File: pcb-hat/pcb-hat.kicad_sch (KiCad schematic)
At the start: 0 parts

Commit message: added SMD buzzer and current sensor
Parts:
- added R1: R_Shunt R010, symbol Device:R_Shunt
- added U1: INA219AxD, Package_SO:SOIC-8_3.9x4.9mm_P1.27mm, symbol Sensor_Energy:INA219AxD
- added U2: ~, symbol PiHatComponents:SMD_buzzer
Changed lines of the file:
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@@
 	(generator_version "9.0")
 	(paper "A4")
+	(symbol
+		(lib_id "Device:R_Shunt")
+		(at 128.27 78.74 0)
+		(unit 1)
+		(exclude_from_sim no)
+		(in_bom yes)
+		(on_board yes)
+		(dnp no)
+		(fields_autoplaced yes)
+		(property "Reference" "R1"
+			(at 125.73 77.4699 0)
+			(effects
+				(font
+					(size 1.27 1.27)
+				)
+				(justify right)
+			)
+		)
+		(property "Value" "R_Shunt R010"
+			(at 125.73 80.0099 0)
+			(effects
+				(font
+					(size 1.27 1.27)
+				)
+				(justify right)
+			)
+		)
+		(property "Footprint" ""
+			(at 126.492 78.74 90)
+			(effects
+				(font
+					(size 1.27 1.27)
+				)
+				(hide yes)
+			)
+		)
+		(property "Datasheet" "~"
+			(at 128.27 78.74 0)
+			(effects
+				(font
+					(size 1.27 1.27)
+				)
+				(hide yes)
+			)
+		)
+		(property "Description" "Shunt resistor with Kelvin connections"
+			(at 128.27 78.74 0)
+			(effects
+				(font
+					(size 1.27 1.27)
+				)
+				(hide yes)
+			)
+		)
+		(pin "2"
+		)
+		(pin "1"
+		)
+		(pin "3"
+		)
+		(pin "4"
+		)
+		(instances
+			(project ""
+				(path "/a3c2d30d-0751-4de7-a899-3d89ad40795d"
+					(reference "R1")
+					(unit 1)
+				)
+			)
+		)
+	)
+	(symbol
+		(lib_id "PiHatComponents:SMD_buzzer")
+		(at 116.84 99.06 0)
+		(unit 1)
+		(exclude_from_sim no)
+		(in_bom yes)
+		(on_board yes)
+		(dnp no)
+		(fields_autoplaced yes)
+		(property "Reference" "U2"
+			(at 133.35 97.1549 0)
+			(effects
+				(font
+					(size 1.27 1.27)
+				)
+				(justify left)
+			)
+		)
+		(property "Value" "~"
+			(at 133.35 99.6949 0)
+			(effects
+				(font
+					(size 1.27 1.27)
+				)
+				(justify left)
+			)
+		)
+		(property "Footprint" ""
+			(at 116.84 99.06 0)
+			(effects
+				(font
+					(size 1.27 1.27)
+				)
+				(hide yes)
+			)
+		)
+		(property "Datasheet" ""
+			(at 116.84 99.06 0)
+			(effects
+				(font
+					(size 1.27 1.27)
+				)
+				(hide yes)
+			)
+		)
+		(property "Description" ""
+			(at 116.84 99.06 0)
+			(effects
+				(font
+					(size 1.27 1.27)
+				)
+				(hide yes)
+			)
+		)
+		(pin "1"
+		)
+		(pin "2"
+		)
+		(instances
+			(project ""
+				(path "/a3c2d30d-0751-4de7-a899-3d89ad40795d"
+					(reference "U2")
+					(unit 1)
+				)
+			)
+		)
+	)
+	(symbol
+		(lib_id "Sensor_Energy:INA219AxD")
+		(at 95.25 78.74 0)
+		(unit 1)
+		(exclude_from_sim no)
+		(in_bom yes)
+		(on_board yes)
+		(dnp no)
+		(fields_autoplaced yes)
+		(property "Reference" "U1"
+			(at 97.3933 66.04 0)
+			(effects
+				(font
+					(size 1.27 1.27)
+				)
+				(justify left)
+			)
+		)
+		(property "Value" "INA219AxD"
+			(at 97.3933 68.58 0)
+			(effects
+				(font
+					(size 1.27 1.27)
+				)
+				(justify left)
+			)
+		)
+		(property "Footprint" "Package_SO:SOIC-8_3.9x4.9mm_P1.27mm"
+			(at 115.57 87.63 0)
+			(effects
+				(font
+					(size 1.27 1.27)
+				)
+				(hide yes)
+			)
+		)
+		(property "Datasheet" "http://www.ti.com/lit/ds/symlink/ina219.pdf"
+			(at 104.14 81.28 0)
+			(effects
+				(font
+					(size 1.27 1.27)
+				)
+				(hide yes)
+			)
+		)
+		(property "Description" "Zero-Drift, Bidirectional Current/Power Monitor (0-26V) With I2C Interface, SOIC-8"
+			(at 95.25 78.74 0)
+			(effects
+				(font
+					(size 1.27 1.27)
+				)
+				(hide yes)
+			)
+		)
+		(pin "8"
+		)
+		(pin "5"
+		)
+		(pin "6"
+		)
+		(pin "3"
+		)
+		(pin "4"
+		)
+		(pin "1"
+		)
+		(pin "2"
+		)
+		(pin "7"
+		)
+		(instances
+			(project ""
+				(path "/a3c2d30d-0751-4de7-a899-3d89ad40795d"
+					(reference "U1")
+					(unit 1)
+				)
+			)
+		)
+	)
 	(sheet_instances
 		(path "/"

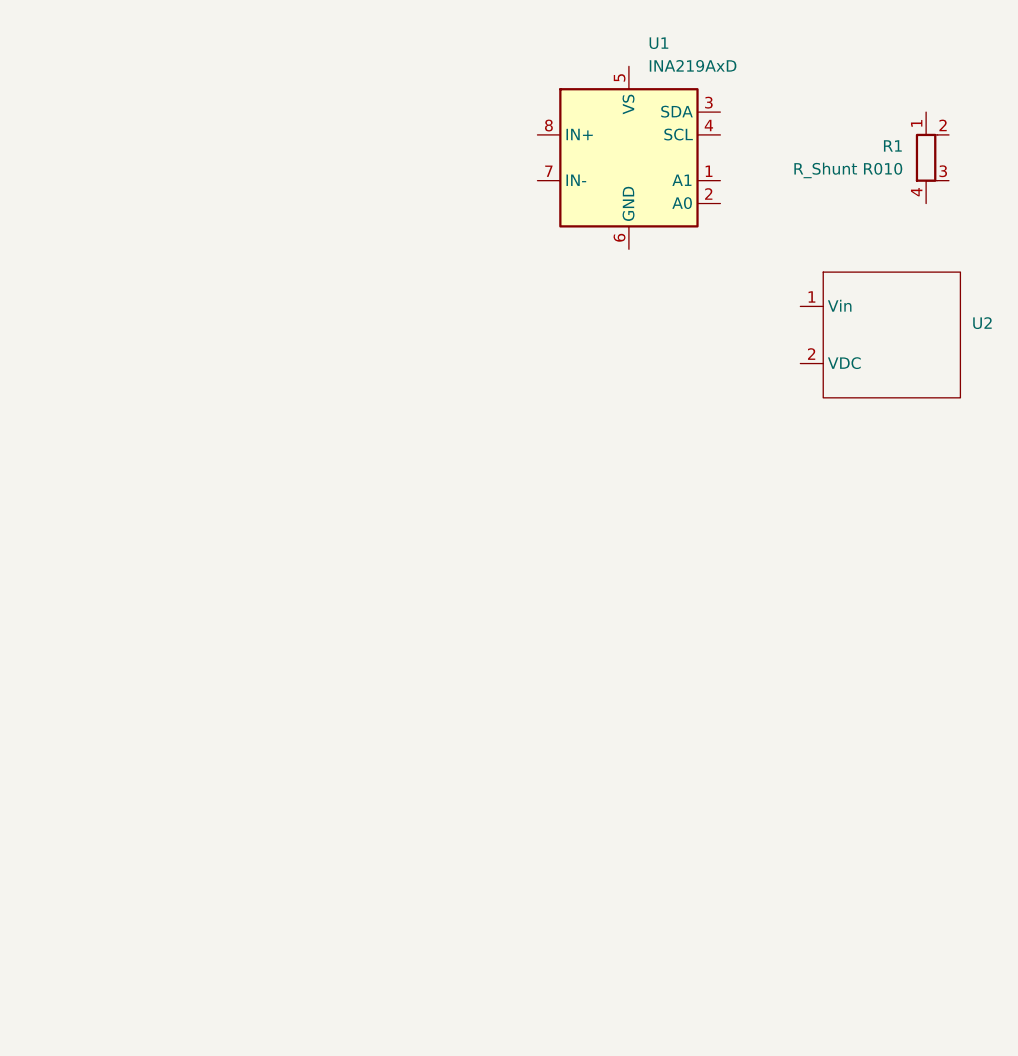
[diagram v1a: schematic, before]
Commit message: Finish current sensor & buzzer wiring
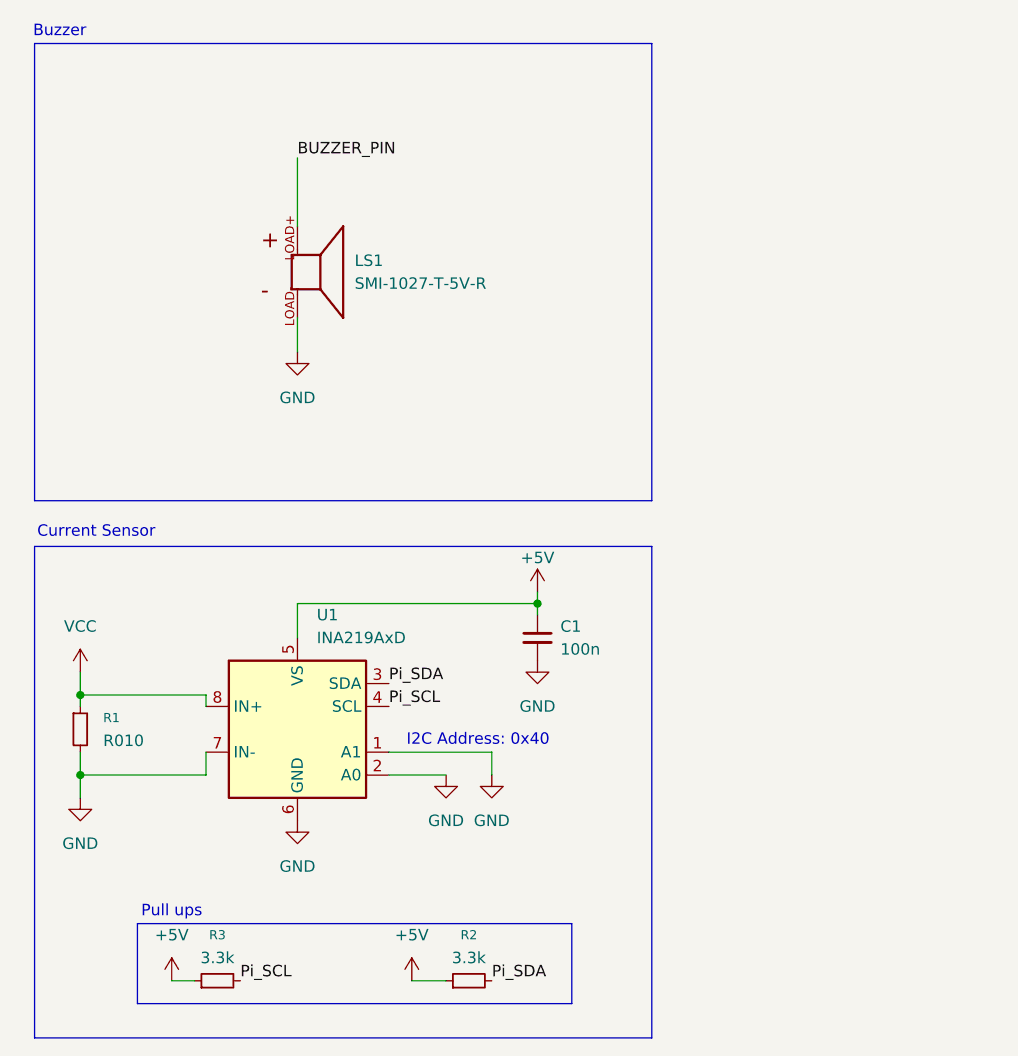
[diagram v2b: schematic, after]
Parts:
- removed R1: R_Shunt R010, symbol Device:R_Shunt
- removed U2: ~, symbol PiHatComponents:SMD_buzzer
- added C1: 100n, Capacitor_SMD:C_0603_1608Metric_Pad1.08x0.95mm_HandSolder, symbol Device:C_Small
- added LS1: SMI-1027-T-5V-R, pcb_hat:XDCR_SMI-1027-T-5V-R, symbol PiHatComponents:SMI-1027-T-5V-R
- added R1: R010, Resistor_SMD:R_0603_1608Metric, symbol Device:R_Small
- added R2, R3: 3.3k, Resistor_SMD:R_0603_1608Metric, symbol Device:R_Small
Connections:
- net GND: now reaches U1.1 (A1)
- net GND: now also U1.2 (A0), U1.6 (GND), U1.7 (IN-), C1.2, LS1.LOAD-, R1.2
- net Pi_SDA: now reaches U1.3 (SDA)
- net Pi_SDA: now also R2.2
- net Pi_SCL: now reaches U1.4 (SCL)
- net Pi_SCL: now also R3.2
- net +5V: now reaches U1.5 (VS)
- net +5V: now also C1.1, R2.1, R3.1
- net VCC: now reaches U1.8 (IN+)
- net VCC: now also R1.1
- new net BUZZER_PIN: LS1.LOAD+
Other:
- note added: "Buzzer"
- note added: "Current Sensor"
- note added: "I2C Address: 0x40"
- note added: "Pull ups"
- moved on the sheet: U1

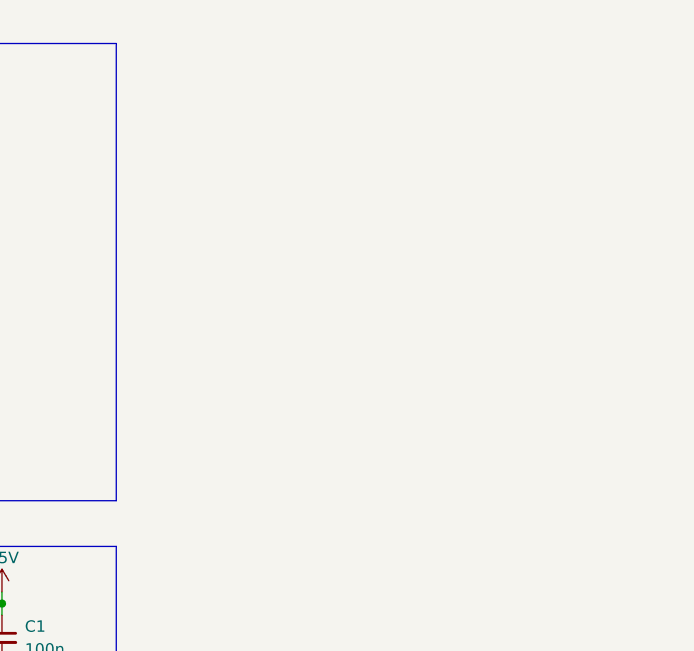
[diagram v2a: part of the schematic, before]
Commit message: 5V Converter sym/footprint and variable regulator sym/footprint/3dmodule added to files
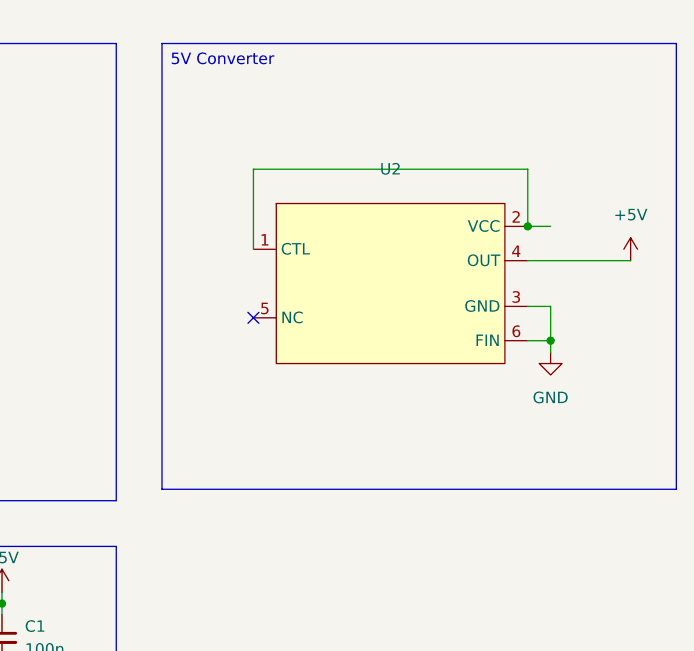
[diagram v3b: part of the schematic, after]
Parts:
- added U2: ~, pcb_hat:DPAK172P1054X200-6N, symbol PiHatComponents:BA50DD0WHFP-TR-HRP-5
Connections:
- net +5V: now also U2.4 (OUT)
- net GND: now also U2.3 (GND), U2.6 (FIN)
- new net: U2.1 (CTL), U2.2 (VCC)
- no-connect marks 0 -> 1

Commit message: Almost finish main voltage regulator
only pot is left
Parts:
- added C2: 1u, Capacitor_SMD:C_0603_1608Metric_Pad1.08x0.95mm_HandSolder, symbol Device:C_Small
- added C3: 22n, Capacitor_SMD:C_0603_1608Metric_Pad1.08x0.95mm_HandSolder, symbol Device:C_Small
- added C4: 0.1u, Capacitor_SMD:C_0603_1608Metric, symbol Device:C_Small
- added C5: 0.012u, Capacitor_SMD:C_0603_1608Metric_Pad1.08x0.95mm_HandSolder, symbol Device:C_Small
- added C6: 47u, Capacitor_SMD:C_1206_3216Metric_Pad1.33x1.80mm_HandSolder, symbol Device:C_Small
- added L1: SRN8040TA-4R7M, pcb_hat:IND_SRN8040TA-4R7M, symbol PiHatComponents:SRN8040TA-4R7M
- added R4: 1R, Resistor_SMD:R_0603_1608Metric, symbol Device:R_Small
- added R5: 75k, Resistor_SMD:R_0603_1608Metric, symbol Device:R_Small
- added R6: 15k, Resistor_SMD:R_0603_1608Metric_Pad0.98x0.95mm_HandSolder, symbol Device:R_Small
- added U3: AOZ6605PI-1, pcb_hat:SOIC127P600X170-9N, symbol PiHatComponents:AOZ6605PI-1
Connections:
- net GND: now also C2.1, C3.2, C5.2, C6.1, R6.1, U3.4 (GND)
- new net: C4.1, R4.2
- new net: C4.2, L1.1, U3.9 (LX)
- new net: C3.1, U3.1 (SS)
- new net: U3.2 (EN), U3.3 (VIN)
- new net: R4.1, U3.5 (BST)
- new net: C2.2, U3.6 (VCC)
- new net: R5.1, U3.7 (COMP)
- new net: R6.2, U3.8 (FB)
- new net: C5.1, R5.2
- new net VDC: C6.2, L1.2
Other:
- note added: "Variable Voltage Regulator"

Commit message: Rearrange stuff
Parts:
- renumbered C3 to C2, C2 to C3, R3 to R2, R2 to R3
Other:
- note added: "PERIPHERIALS"
- note added: "POWER"
- note removed: "Buzzer"
- note removed: "Current Sensor"
- note removed: "Variable Voltage Regulator"
- title: (none) -> Pi Hat
- moved on the sheet: C1, C2, C3, C4, C5, C6, L1, LS1, R1, R2, R3, R4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

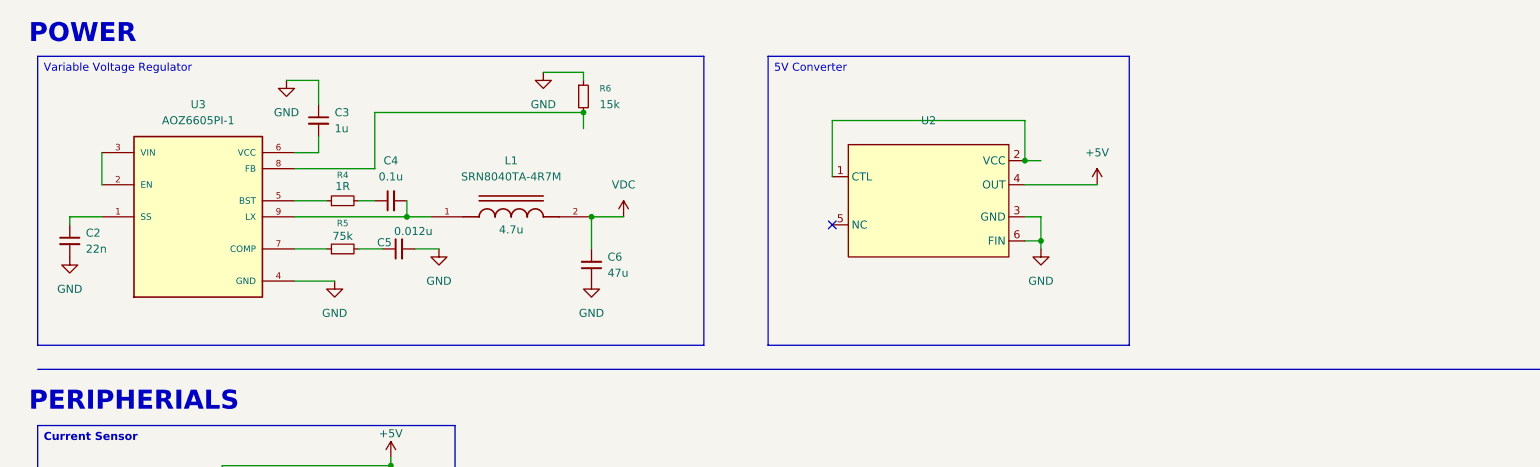
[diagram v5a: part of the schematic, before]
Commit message: Added solder jumps and resistors
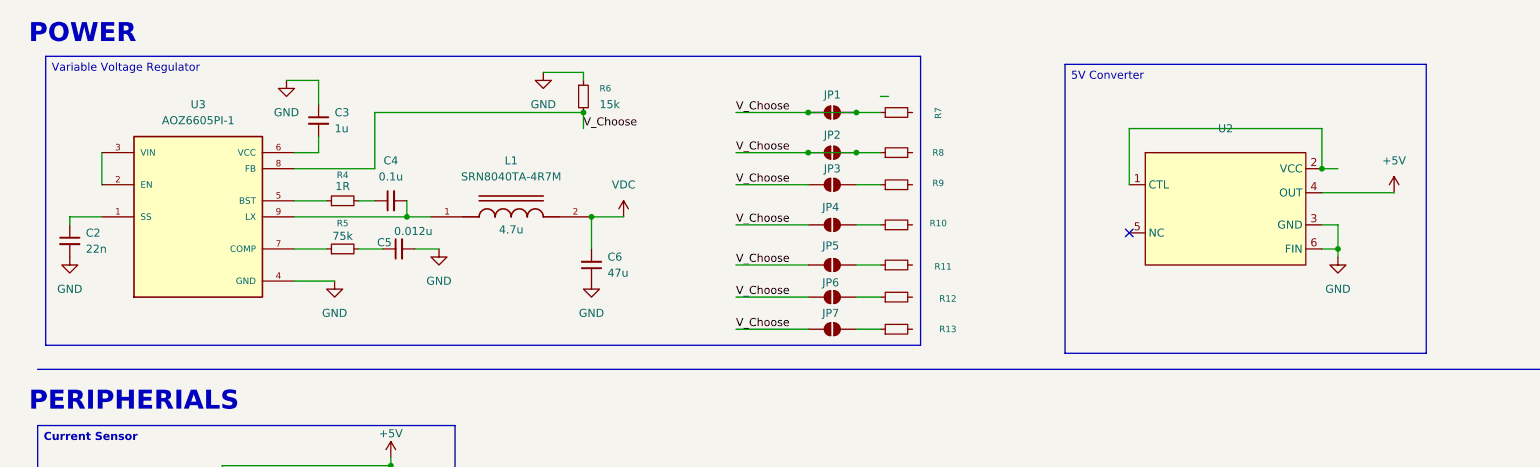
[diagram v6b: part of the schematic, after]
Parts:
- added JP1, JP2, JP3, JP4, JP5, JP6, JP7: SolderJumper_2_Open, Jumper:SolderJumper-2_P1.3mm_Open_RoundedPad1.0x1.5mm, symbol Jumper:SolderJumper_2_Open
- added R10, R11, R12, R13, R8, R9: R_Small, Resistor_SMD:R_0603_1608Metric_Pad0.98x0.95mm_HandSolder, symbol Device:R_Small
- added R7: R_Small, Resistor_SMD:R_0201_0603Metric_Pad0.64x0.40mm_HandSolder, symbol Device:R_Small
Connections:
- net V_Choose: now reaches R6.2, U3.8 (FB)
- net V_Choose: now also JP1.1 (A), JP1.2 (B), JP2.1 (A), JP2.2 (B), JP3.1 (A), JP4.1 (A), JP5.1 (A), JP6.1 (A), JP7.1 (A), R7.1, R8.1
- new net: JP6.2 (B), R12.1
- new net: JP7.2 (B), R13.1
- new net: JP5.2 (B), R11.1
- new net: JP3.2 (B), R9.1
- new net: JP4.2 (B), R10.1
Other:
- moved on the sheet: U2

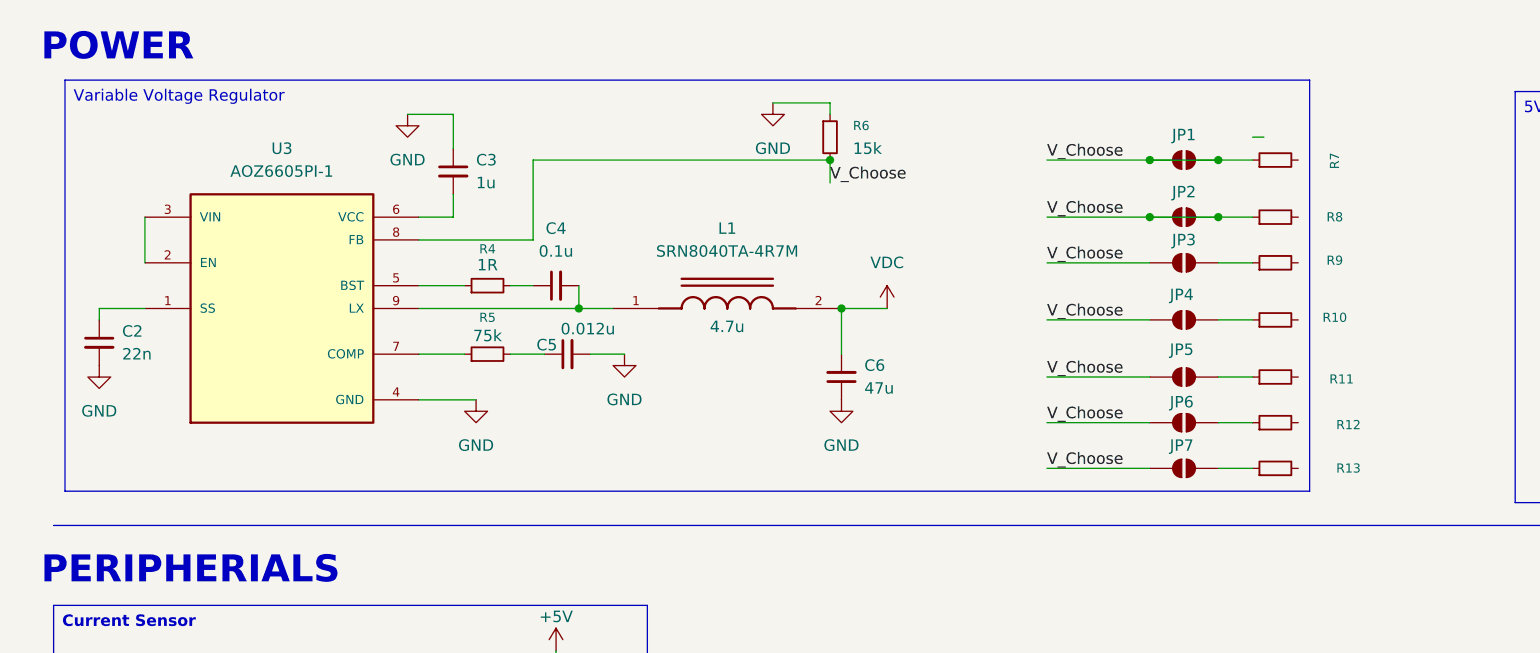
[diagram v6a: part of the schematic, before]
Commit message: Resistance values and Decoupling capacitor added
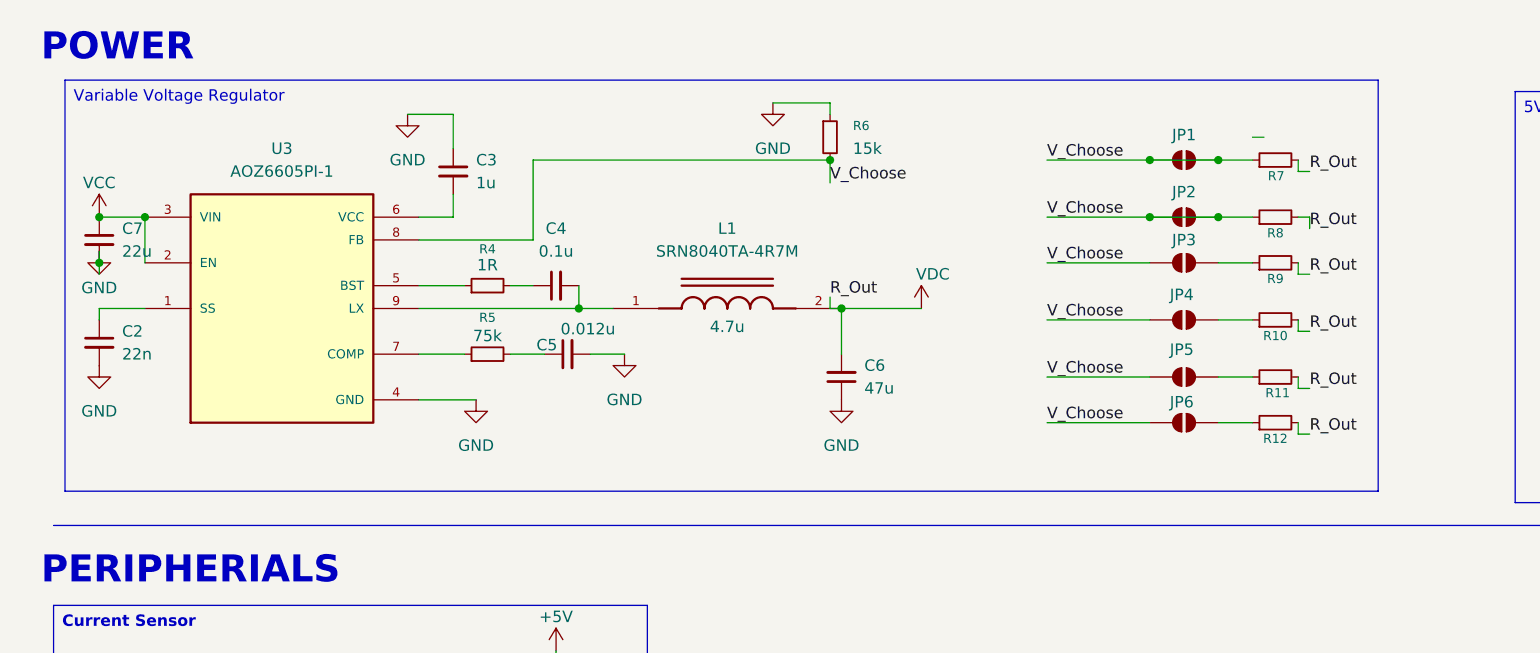
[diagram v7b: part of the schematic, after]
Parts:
- removed JP7: SolderJumper_2_Open, Jumper:SolderJumper-2_P1.3mm_Open_RoundedPad1.0x1.5mm, symbol Jumper:SolderJumper_2_Open
- removed R13: R_Small, Resistor_SMD:R_0603_1608Metric_Pad0.98x0.95mm_HandSolder, symbol Device:R_Small
- added C7: 22u, Capacitor_SMD:C_0603_1608Metric, symbol Device:C_Small
- R10: value R_Small -> 285k
- R11: value R_Small -> 310k
- R12: value R_Small -> 335k
- R7: value R_Small -> 210k
- R8: value R_Small -> 235k
- R9: value R_Small -> 260k
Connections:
- net GND: now also C7.2
- net VCC: now also U3.2 (EN), U3.3 (VIN), C7.1
- net VDC: now also R10.2, R11.2, R12.2, R7.2, R8.2, R9.2
